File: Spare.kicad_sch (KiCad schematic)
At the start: 9 parts, among them U11 74LS06, U12 74LS00, U13 74LS74, U19 74HCT74, U20 74LS74, U21 74LS14, U22 74LS06, U4 74LS86, U7 74LS32

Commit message: Schematic in progress
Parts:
- removed U11: 74LS06, DIP-14__300, symbol 74xx:74LS06
- removed U13: 74LS74, symbol 74xx:74LS74
- removed U19: 74HCT74, DIP-14__300, symbol 74xx:74LS74
- removed U20: 74LS74, DIP-14__300, symbol 74xx:74LS74
- removed unit 1 of U21
- removed unit 6 of U22
- removed U7: 74LS32, DIP-14__300, symbol 74xx:74LS32
- added U10: 74LS32, Package_DIP:DIP-14_W7.62mm_Socket_LongPads, symbol 74xx:74LS32
- added U13: 74LS07, Package_DIP:DIP-14_W7.62mm_Socket_LongPads, symbol 74xx:74LS07
- added unit 4 of U17
- added U20: 74LS04, Package_DIP:DIP-14_W7.62mm_Socket_LongPads, symbol 74xx:74LS04
- U17: renamed from U21; footprint DIP-14__300 -> Package_DIP:DIP-14_W7.62mm_Socket_LongPads
- U18: renamed from U22; footprint DIP-14__300 -> Package_DIP:DIP-14_W7.62mm_Socket_LongPads
- U21: renamed from U12; footprint DIP-14__300 -> Package_DIP:DIP-14_W7.62mm_Socket_LongPads
- U4: footprint DIP-14__300 -> Package_DIP:DIP-14_W7.62mm_Socket_LongPads
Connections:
- no-connect marks 53 -> 44
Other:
- company: N8VEM Users Group -> (none)
- title: 6809 and 6502 ATX and 6U -> 6809PC
- moved on the sheet: U17C, U17E, U17F, U18A, U18B, U18C, U21D, U4D

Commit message: PCB in progress
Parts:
- removed U10: 74LS32, Package_DIP:DIP-14_W7.62mm_Socket_LongPads, symbol 74xx:74LS32
- added U15: 74LS08, Custom:STD_DDW_DIP14, symbol 74xx:74LS08
- U13, U17, U18, U20, U21, U4: footprint Package_DIP:DIP-14_W7.62mm_Socket_LongPads -> Custom:STD_DDW_DIP14
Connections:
- no-connect marks 44 -> 41
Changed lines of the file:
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@@
-	)
-	(no_connect
-		(at 252.73 123.19)
 	)
 	(no_connect
@@
 	)
 	(no_connect
-		(at 252.73 118.11)
+		(at 196.85 118.11)
 	)
 	(no_connect
@@
 	)
 	(no_connect
+		(at 196.85 113.03)
+	)
+	(no_connect
 		(at 196.85 160.02)
 	)
@@
 	)
 	(no_connect
+		(at 212.09 115.57)
+	)
+	(no_connect
 		(at 266.7 152.4)
 	)
@@
 	)
 	(no_connect
-		(at 267.97 134.62)
-	)
-	(no_connect
 		(at 237.49 88.9)
 	)
@@
 	)
 	(no_connect
-		(at 252.73 132.08)
-	)
-	(no_connect
 		(at 266.7 179.07)
 	)
 	(no_connect
-		(at 267.97 120.65)
-	)
-	(no_connect
 		(at 254 100.33)
 	)
 	(no_connect
 		(at 266.7 166.37)
-	)
-	(no_connect
-		(at 252.73 137.16)
 	)
 	(no_connect
@@
 			)
 		)
-		(property "Footprint" "Package_DIP:DIP-14_W7.62mm_Socket_LongPads"
+		(property "Footprint" "Custom:STD_DDW_DIP14"
 			(at 261.62 102.87 0)
 			(effects
@@
 			)
 		)
-		(property "Footprint" "Package_DIP:DIP-14_W7.62mm_Socket_LongPads"
+		(property "Footprint" "Custom:STD_DDW_DIP14"
 			(at 204.47 149.86 0)
 			(effects
@@
 			)
 		)
-		(property "Footprint" "Package_DIP:DIP-14_W7.62mm_Socket_LongPads"
+		(property "Footprint" "Custom:STD_DDW_DIP14"
 			(at 204.47 160.02 0)
 			(effects
@@
 			)
 		)
-		(property "Footprint" "Package_DIP:DIP-14_W7.62mm_Socket_LongPads"
+		(property "Footprint" "Custom:STD_DDW_DIP14"
 			(at 260.35 90.17 0)
 			(effects
@@
 			)
 		)
-		(property "Footprint" "Package_DIP:DIP-14_W7.62mm_Socket_LongPads"
+		(property "Footprint" "Custom:STD_DDW_DIP14"
 			(at 232.41 154.94 0)
 			(effects
@@
 	)
 	(symbol
-		(lib_id "74xx:74LS32")
-		(at 260.35 134.62 0)
-		(unit 4)
-		(exclude_from_sim no)
-		(in_bom yes)
-		(on_board yes)
-		(dnp no)
-		(fields_autoplaced yes)
-		(property "Reference" "U10"
-			(at 260.35 125.73 0)
-			(effects
-				(font
-					(size 1.27 1.27)
-				)
-			)
-		)
-		(property "Value" "74LS32"
-			(at 260.35 128.27 0)
-			(effects
-				(font
-					(size 1.27 1.27)
-				)
-			)
-		)
-		(property "Footprint" "Package_DIP:DIP-14_W7.62mm_Socket_LongPads"
-			(at 260.35 134.62 0)
-			(effects
-				(font
-					(size 1.27 1.27)
-				)
-				(hide yes)
-			)
-		)
-		(property "Datasheet" "http://www.ti.com/lit/gpn/sn74LS32"
-			(at 260.35 134.62 0)
-			(effects
-				(font
-					(size 1.27 1.27)
-				)
-				(hide yes)
-			)
-		)
-		(property "Description" "Quad 2-input OR"
-			(at 260.35 134.62 0)
-			(effects
-				(font
-					(size 1.27 1.27)
-				)
-				(hide yes)
-			)
-		)
-		(pin "8"
-		)
-		(pin "6"
-		)
-		(pin "3"
-		)
-		(pin "11"
-		)
-		(pin "12"
-		)
-		(pin "13"
-		)
-		(pin "14"
-		)
-		(pin "5"
-		)
-		(pin "10"
-		)
-		(pin "2"
-		)
-		(pin "9"
-		)
-		(pin "1"
-		)
-		(pin "4"
-		)
-		(pin "7"
-		)
-		(instances
-			(project "6809PC-6U"
-				(path "/d94f9d60-5ece-4752-b49c-b0d1c95f35bc/00000000-0000-0000-0000-0000526d48aa"
-					(reference "U10")
-					(unit 4)
-				)
-			)
-		)
-	)
-	(symbol
 		(lib_id "74xx:74LS04")
 		(at 259.08 166.37 0)
@@
 			)
 		)
-		(property "Footprint" "Package_DIP:DIP-14_W7.62mm_Socket_LongPads"
+		(property "Footprint" "Custom:STD_DDW_DIP14"
 			(at 259.08 166.37 0)
 			(effects
@@
 			)
 		)
-		(property "Footprint" "Package_DIP:DIP-14_W7.62mm_Socket_LongPads"
+		(property "Footprint" "Custom:STD_DDW_DIP14"
 			(at 229.87 88.9 0)
 			(effects
@@
 			)
 		)
-		(property "Footprint" "Package_DIP:DIP-14_W7.62mm_Socket_LongPads"
+		(property "Footprint" "Custom:STD_DDW_DIP14"
 			(at 259.08 179.07 0)
 			(effects
@@
 			)
 		)
-		(property "Footprint" "Package_DIP:DIP-14_W7.62mm_Socket_LongPads"
+		(property "Footprint" "Custom:STD_DDW_DIP14"
 			(at 204.47 129.54 0)
 			(effects
@@
 			)
 		)
-		(property "Footprint" "Package_DIP:DIP-14_W7.62mm_Socket_LongPads"
+		(property "Footprint" "Custom:STD_DDW_DIP14"
 			(at 232.41 146.05 0)
 			(effects
@@
 	)
 	(symbol
-		(lib_id "74xx:74LS32")
-		(at 260.35 120.65 0)
-		(unit 3)
-		(exclude_from_sim no)
-		(in_bom yes)
-		(on_board yes)
-		(dnp no)
-		(fields_autoplaced yes)
-		(property "Reference" "U10"
-			(at 260.35 111.76 0)
-			(effects
-				(font
-					(size 1.27 1.27)
-				)
-			)
-		)
-		(property "Value" "74LS32"
-			(at 260.35 114.3 0)
-			(effects
-				(font
-					(size 1.27 1.27)
-				)
-			)
-		)
-		(property "Footprint" "Package_DIP:DIP-14_W7.62mm_Socket_LongPads"
-			(at 260.35 120.65 0)
-			(effects
-				(font
-					(size 1.27 1.27)
-				)
-				(hide yes)
-			)
-		)
-		(property "Datasheet" "http://www.ti.com/lit/gpn/sn74LS32"
-			(at 260.35 120.65 0)
-			(effects
-				(font
-					(size 1.27 1.27)
-				)
-				(hide yes)
-			)
-		)
-		(property "Description" "Quad 2-input OR"
-			(at 260.35 120.65 0)
-			(effects
-				(font
-					(size 1.27 1.27)
-				)
-				(hide yes)
-			)
+		(lib_id "74xx:74LS08")
+		(at 204.47 115.57 0)
+		(unit 4)
+		(convert 2)
+		(exclude_from_sim no)
+		(in_bom yes)
+		(on_board yes)
+		(dnp no)
+		(property "Reference" "U15"
+			(at 204.47 114.3 0)
+			(effects
+				(font
+					(size 1.524 1.524)
+				)
+			)
+		)
+		(property "Value" "74LS08"
+			(at 204.47 116.84 0)
+			(effects
+				(font
+					(size 1.524 1.524)
+				)
+			)
+		)
+		(property "Footprint" "Custom:STD_DDW_DIP14"
+			(at 204.47 115.57 0)
+			(effects
+				(font
+					(size 1.27 1.27)
+				)
+				(hide yes)
+			)
+		)
+		(property "Datasheet" "http://www.ti.com/lit/gpn/sn74LS08"
+			(at 204.47 115.57 0)
+			(effects
+				(font
+					(size 1.27 1.27)
+				)
+				(hide yes)
+			)
+		)
+		(property "Description" "Quad And2"
+			(at 204.47 115.57 0)
+			(effects
+				(font
+					(size 1.27 1.27)
+				)
+				(hide yes)
+			)
+		)
+		(pin "14"
+		)
+		(pin "7"
+		)
+		(pin "1"
+		)
+		(pin "2"
+		)
+		(pin "10"
 		)
 		(pin "8"
 		)
+		(pin "12"
+		)
+		(pin "4"
+		)
+		(pin "9"
+		)
 		(pin "6"
 		)
+		(pin "5"
+		)
 		(pin "3"
 		)
+		(pin "13"
+		)
 		(pin "11"
-		)
-		(pin "12"
-		)
-		(pin "13"
-		)
-		(pin "14"
-		)
-		(pin "5"
-		)
-		(pin "10"
-		)
-		(pin "2"
-		)
-		(pin "9"
-		)
-		(pin "1"
-		)
-		(pin "4"
-		)
-		(pin "7"
 		)
 		(instances
 			(project "6809PC-6U"
 				(path "/d94f9d60-5ece-4752-b49c-b0d1c95f35bc/00000000-0000-0000-0000-0000526d48aa"
-					(reference "U10")
-					(unit 3)
+					(reference "U15")
+					(unit 4)
 				)
 			)
@@
 			)
 		)
-		(property "Footprint" "Package_DIP:DIP-14_W7.62mm_Socket_LongPads"
+		(property "Footprint" "Custom:STD_DDW_DIP14"
 			(at 232.41 173.99 0)
 			(effects
@@
 			)
 		)
-		(property "Footprint" "Package_DIP:DIP-14_W7.62mm_Socket_LongPads"
+		(property "Footprint" "Custom:STD_DDW_DIP14"
 			(at 204.47 139.7 0)
 			(effects
@@
 			)
 		)
-		(property "Footprint" "Package_DIP:DIP-14_W7.62mm_Socket_LongPads"
+		(property "Footprint" "Custom:STD_DDW_DIP14"
 			(at 232.41 137.16 0)
 			(effects
@@
 			)
 		)
-		(property "Footprint" "Package_DIP:DIP-14_W7.62mm_Socket_LongPads"
+		(property "Footprint" "Custom:STD_DDW_DIP14"
 			(at 259.08 191.77 0)
 			(effects
@@
 			)
 		)
-		(property "Footprint" "Package_DIP:DIP-14_W7.62mm_Socket_LongPads"
+		(property "Footprint" "Custom:STD_DDW_DIP14"
 			(at 259.08 152.4 0)
 			(effects
@@
 			)
 		)
-		(property "Footprint" "Package_DIP:DIP-14_W7.62mm_Socket_LongPads"
+		(property "Footprint" "Custom:STD_DDW_DIP14"
 			(at 232.41 163.83 0)
 			(effects
@@
 			)
 		)
-		(property "Footprint" "Package_DIP:DIP-14_W7.62mm_Socket_LongPads"
+		(property "Footprint" "Custom:STD_DDW_DIP14"
 			(at 229.87 101.6 0)
 			(effects
@@
 			)
 		)
-		(property "Footprint" "Package_DIP:DIP-14_W7.62mm_Socket_LongPads"
+		(property "Footprint" "Custom:STD_DDW_DIP14"
 			(at 229.87 115.57 0)
 			(effects

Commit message: 6809PC work
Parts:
- removed U13: 74LS07, Custom:STD_DDW_DIP14, symbol 74xx:74LS07
- removed U20: 74LS04, Custom:STD_DDW_DIP14, symbol 74xx:74LS04
- added U10, U16: 74LS32, Custom:STD_DDW_DIP14, symbol 74xx:74LS32
- added unit 2 of U4
- added U5: 74LS02, Custom:STD_DDW_DIP14, symbol 74xx:74LS02
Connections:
- no-connect marks 41 -> 38

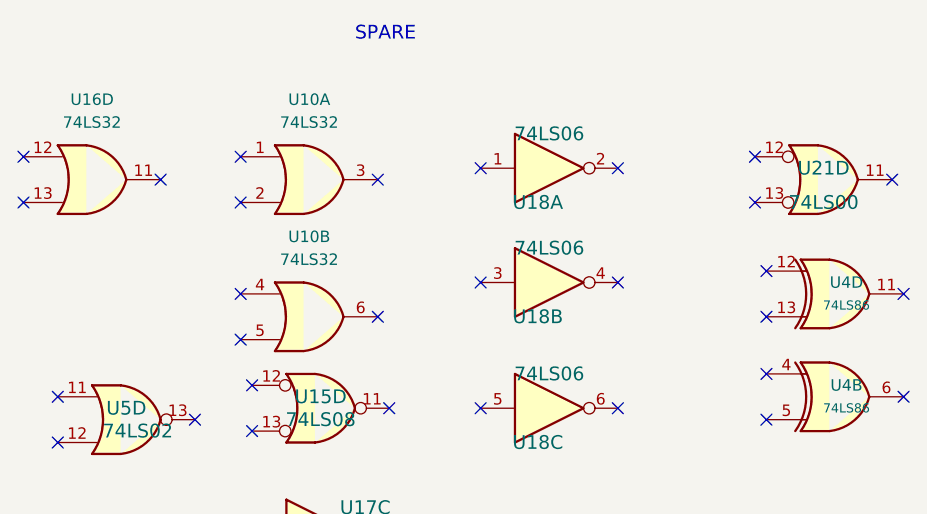
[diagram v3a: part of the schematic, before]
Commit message: fix issue with ISA RW select lines
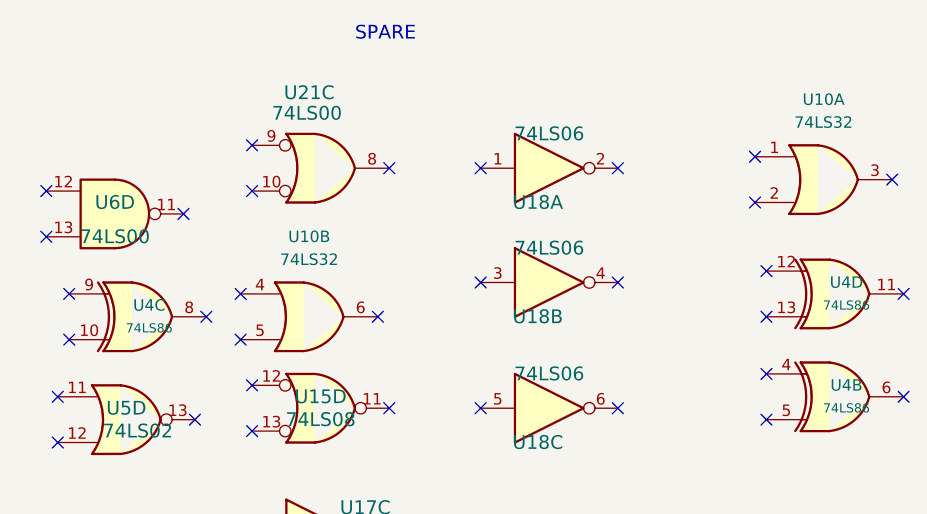
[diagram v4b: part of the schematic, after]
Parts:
- removed U16: 74LS32, Custom:STD_DDW_DIP14, symbol 74xx:74LS32
- removed U21: 74LS00, Custom:STD_DDW_DIP14, symbol 74xx:74LS00
- added U21, U6: 74LS00, Custom:STD_DDW_DIP14, symbol 74xx:74LS00
- added unit 3 of U4
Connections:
- no-connect marks 38 -> 41

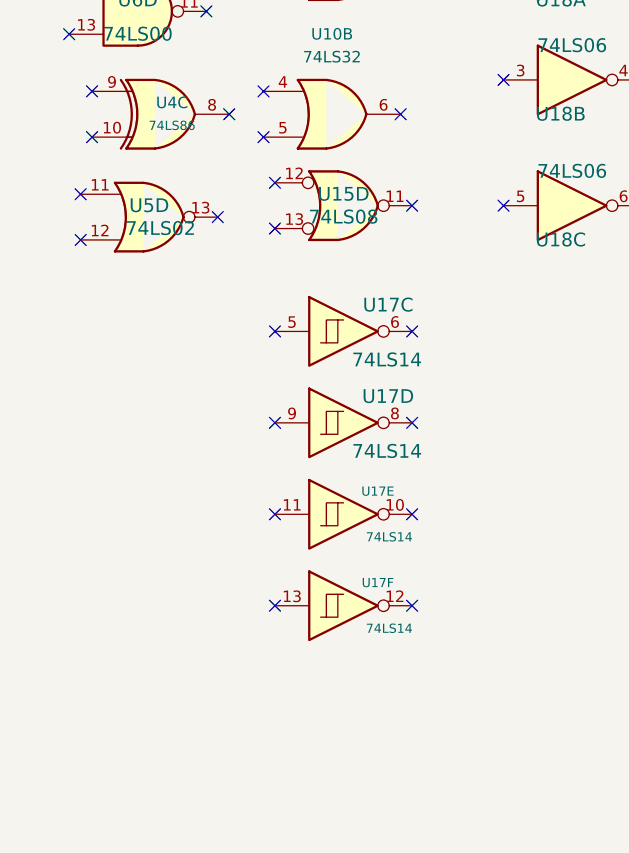
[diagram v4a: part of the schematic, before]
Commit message: fix bus issue
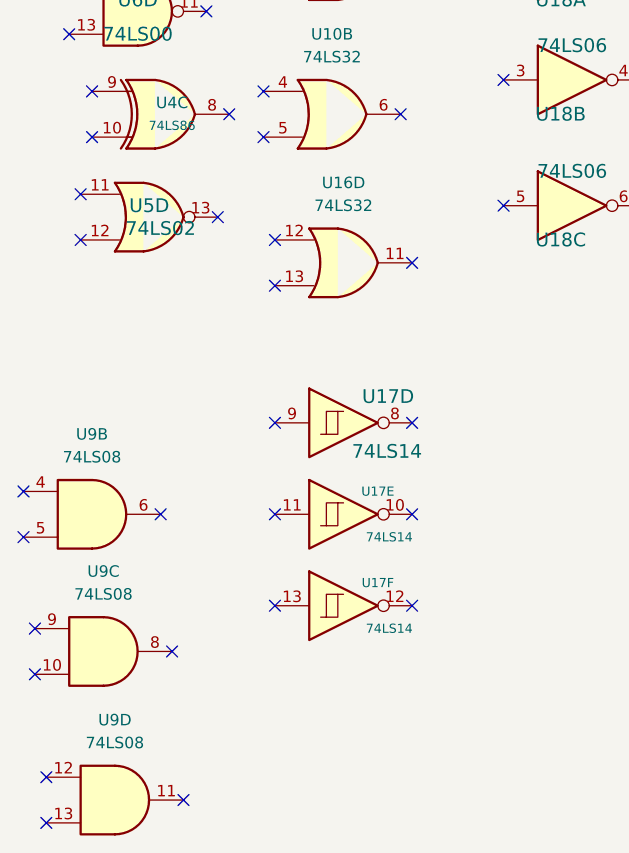
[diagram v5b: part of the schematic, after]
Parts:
- removed U15: 74LS08, Custom:STD_DDW_DIP14, symbol 74xx:74LS08
- removed unit 3 of U17
- added U16: 74LS32, Custom:STD_DDW_DIP14, symbol 74xx:74LS32
- added U9: 74LS08, Custom:STD_DDW_DIP14, symbol 74xx:74LS08
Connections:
- no-connect marks 41 -> 48

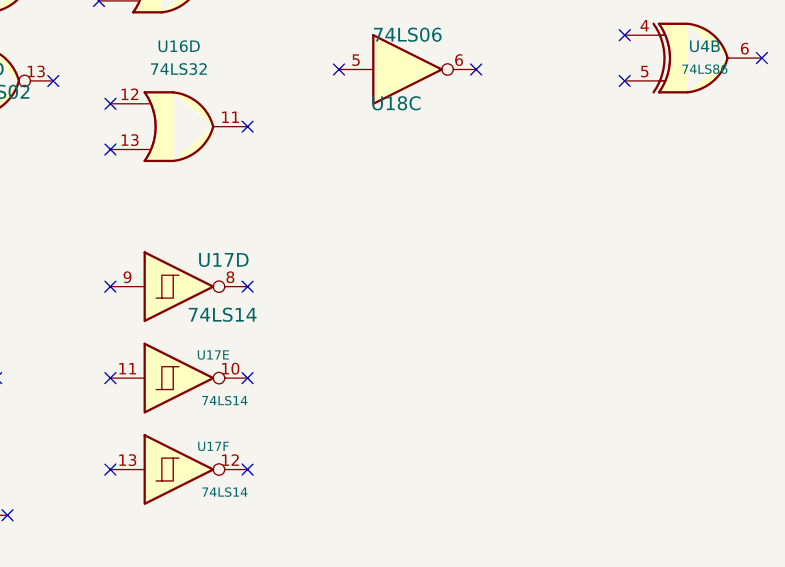
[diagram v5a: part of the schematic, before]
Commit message: fix power supply switch circuit
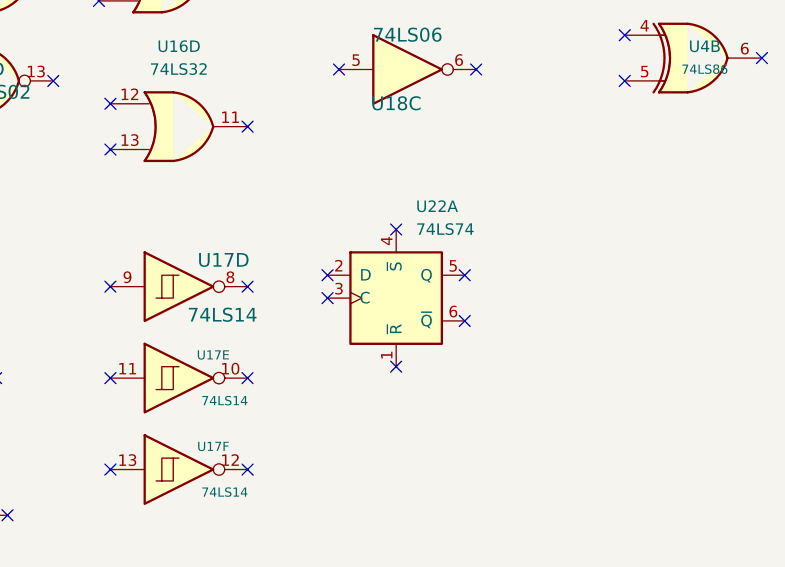
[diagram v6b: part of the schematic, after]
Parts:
- added U22: 74LS74, Custom:STD_DDW_DIP14, symbol 74xx:74LS74
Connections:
- no-connect marks 48 -> 54
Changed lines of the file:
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@@
 	(title_block
 		(title "6809PC")
-		(date "2025-05-31")
-		(rev "003")
+		(date "2025-06-20")
+		(rev "004")
 		(comment 1 "https://github.com/danwerner21/6809PC")
 		(comment 2 "Based on work by Andrew Lynch and John Coffman")
@@
 	)
 	(no_connect
+		(at 228.6 148.59)
+	)
+	(no_connect
 		(at 184.15 149.86)
 	)
@@
 	)
 	(no_connect
+		(at 220.98 140.97)
+	)
+	(no_connect
+		(at 228.6 133.35)
+	)
+	(no_connect
 		(at 212.09 88.9)
 	)
@@
 	)
 	(no_connect
+		(at 236.22 138.43)
+	)
+	(no_connect
 		(at 176.53 107.95)
 	)
@@
 	)
 	(no_connect
+		(at 236.22 143.51)
+	)
+	(no_connect
 		(at 186.69 181.61)
 	)
@@
 	(no_connect
 		(at 196.85 124.46)
+	)
+	(no_connect
+		(at 220.98 138.43)
 	)
 	(no_connect
@@
 				)
 			)
+		)
+	)
+	(symbol
+		(lib_id "74xx:74LS74")
+		(at 228.6 140.97 0)
+		(unit 1)
+		(exclude_from_sim no)
+		(in_bom yes)
+		(on_board yes)
+		(dnp no)
+		(fields_autoplaced yes)
+		(property "Reference" "U22"
+			(at 230.7941 130.81 0)
+			(effects
+				(font
+					(size 1.27 1.27)
+				)
+				(justify left)
+			)
+		)
+		(property "Value" "74LS74"
+			(at 230.7941 133.35 0)
+			(effects
+				(font
+					(size 1.27 1.27)
+				)
+				(justify left)
+			)
+		)
+		(property "Footprint" "Custom:STD_DDW_DIP14"
+			(at 228.6 140.97 0)
+			(effects
+				(font
+					(size 1.27 1.27)
+				)
+				(hide yes)
+			)
+		)
+		(property "Datasheet" "74xx/74hc_hct74.pdf"
+			(at 228.6 140.97 0)
+			(effects
+				(font
+					(size 1.27 1.27)
+				)
+				(hide yes)
+			)
+		)
+		(property "Description" "Dual D Flip-flop, Set & Reset"
+			(at 228.6 140.97 0)
+			(effects
+				(font
+					(size 1.27 1.27)
+				)
+				(hide yes)
+			)
+		)
+		(pin "5"
+		)
+		(pin "13"
+		)
+		(pin "8"
+		)
+		(pin "9"
+		)
+		(pin "2"
+		)
+		(pin "1"
+		)
+		(pin "3"
+		)
+		(pin "4"
+		)
+		(pin "10"
+		)
+		(pin "6"
+		)
+		(pin "11"
+		)
+		(pin "12"
+		)
+		(pin "7"
+		)
+		(pin "14"
+		)
+		(instances
+			(project "6809PC-6U"
+				(path "/d94f9d60-5ece-4752-b49c-b0d1c95f35bc/00000000-0000-0000-0000-0000526d48aa"
+					(reference "U22")
+					(unit 1)
+				)
+			)

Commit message: isa work
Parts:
- removed unit 4 of U17
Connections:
- no-connect marks 54 -> 52
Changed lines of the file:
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@@
-	)
-	(no_connect
-		(at 212.09 139.7)
 	)
 	(no_connect
@@
 	(no_connect
 		(at 212.09 160.02)
-	)
-	(no_connect
-		(at 196.85 139.7)
 	)
 	(no_connect
@@
 					(unit 4)
 				)
-			)
-		)
-	)
-	(symbol
-		(lib_id "74xx:74LS14")
-		(at 204.47 139.7 0)
-		(unit 4)
-		(exclude_from_sim no)
-		(in_bom yes)
-		(on_board yes)
-		(dnp no)
-		(property "Reference" "U17"
-			(at 209.423 136.779 0)
-			(effects
-				(font
-					(size 1.524 1.524)
-				)
-			)
-		)
-		(property "Value" "74LS14"
-			(at 209.296 142.875 0)
-			(effects
-				(font
-					(size 1.524 1.524)
-				)
-			)
-		)
-		(property "Footprint" "Custom:STD_DDW_DIP14"
-			(at 204.47 139.7 0)
-			(effects
-				(font
-					(size 1.27 1.27)
-				)
-				(hide yes)
-			)
-		)
-		(property "Datasheet" "http://www.ti.com/lit/gpn/sn74LS14"
-			(at 204.47 139.7 0)
-			(effects
-				(font
-					(size 1.27 1.27)
-				)
-				(hide yes)
-			)
-		)
-		(property "Description" "Hex inverter schmitt trigger"
-			(at 204.47 139.7 0)
-			(effects
-				(font
-					(size 1.27 1.27)
-				)
-				(hide yes)
-			)
-		)
-		(pin "2"
-		)
-		(pin "8"
-		)
-		(pin "7"
-		)
-		(pin "9"
-		)
-		(pin "14"
-		)
-		(pin "1"
-		)
-		(pin "4"
-		)
-		(pin "3"
-		)
-		(pin "6"
-		)
-		(pin "5"
-		)
-		(pin "12"
-		)
-		(pin "13"
-		)
-		(pin "11"
-		)
-		(pin "10"
-		)
-		(instances
-			(project "6809PC-6U"
-				(path "/d94f9d60-5ece-4752-b49c-b0d1c95f35bc/00000000-0000-0000-0000-0000526d48aa"
-					(reference "U17")
-					(unit 4)
-				)
